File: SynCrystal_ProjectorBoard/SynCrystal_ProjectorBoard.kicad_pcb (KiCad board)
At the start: 2 copper layers, 59.7 x 25.4 mm, 19 parts, among them J1 to Motor Ctrl PCB, J2 to DIN Connector, J3 to Lamp Relay Board, J4 to DIN Socket, J5 Relais Board, J6 uC Cable, U1 AP63205WU, U2 TS5A3160DBVR-TP, U3 TS5A3160DBVR-TP, U4 TS5A3160DBVR-TP

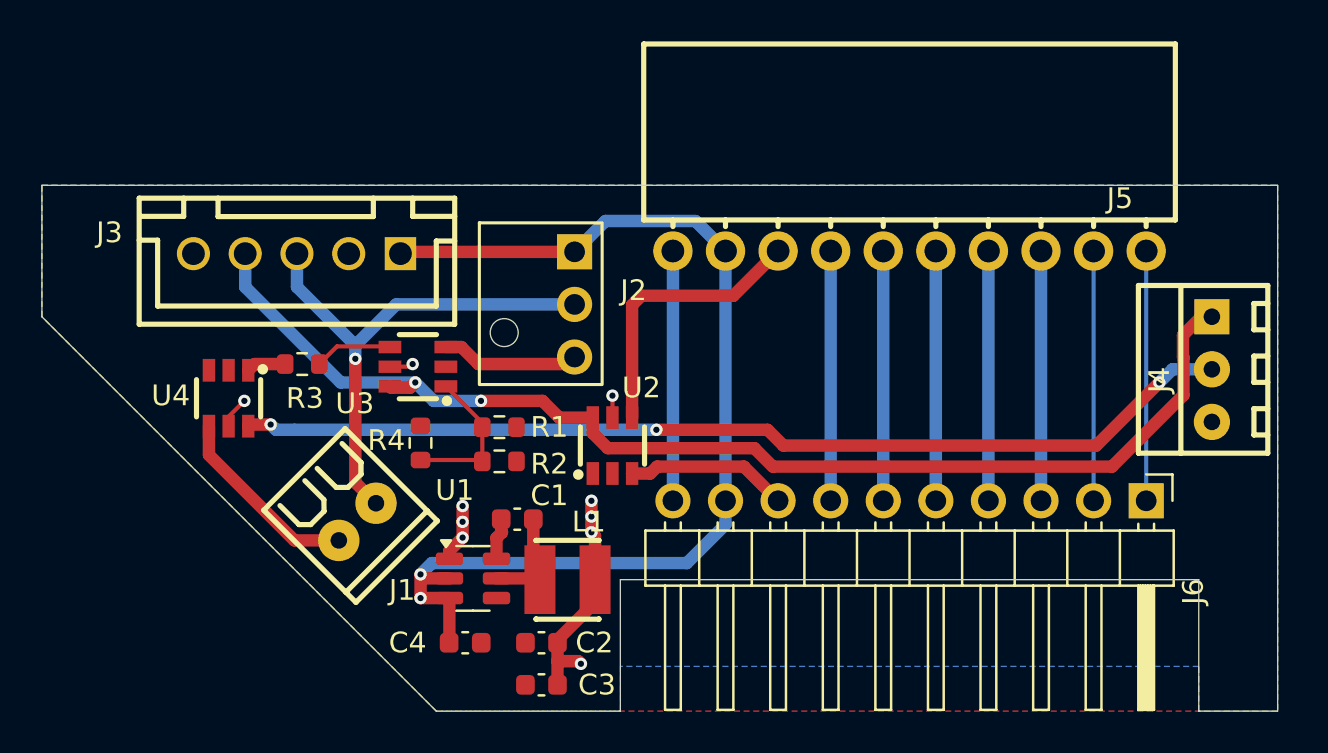
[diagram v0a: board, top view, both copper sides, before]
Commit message: DRC for Projector Board happy
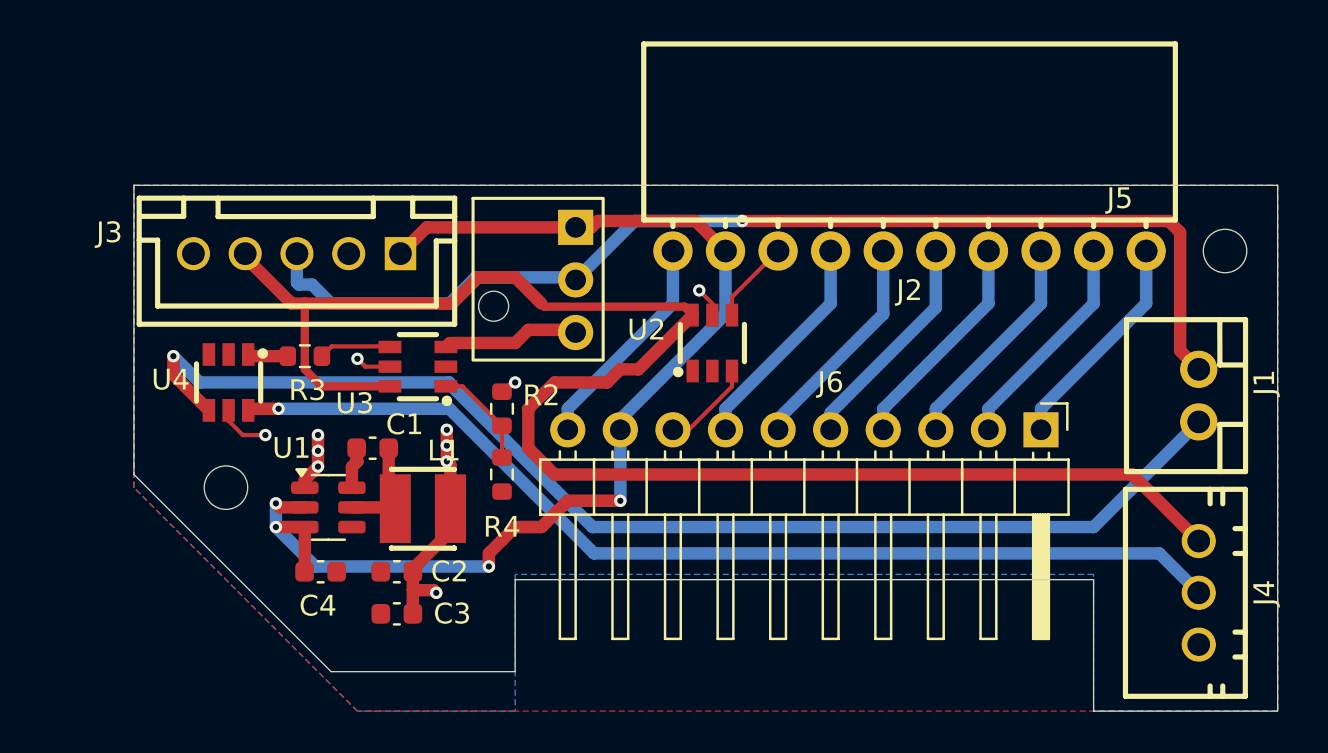
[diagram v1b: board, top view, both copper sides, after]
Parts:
- removed R1: 16k5, Resistor_SMD:R_0603_1608Metric
- added H1: MountingHole, Peacemans Teile:MountingHole_2.1mm_just_hole, F.Cu at (167.6, 90.8)
- added H2: MountingHole, Peacemans Teile:MountingHole_2.1mm_just_hole, F.Cu at (215.9, 79.4)
- J1: footprint easyEDA:CONN-TH_2P-P2.54_MX128-2.54-GN01-02P-CU-Y-A -> easyEDA:CONN-TH_2P-P2.54_ZX-XH2.54-2PZZ-Y
- J4: footprint easyEDA:CONN-TH_3P-P2.54_MX128-2.54-03P-GN01-CU-Y-A -> easyEDA:CONN-TH_ZX-XH2.54-3PZZ-Y
- R2: value 5k1 -> 6k8
- R4: value 1k6 -> 2k7
- moved J1 41.1 mm to (214.6, 86.4), turned to 90 degrees
- moved J4 10.8 mm to (214.6, 95.9)
- moved C4 7.78 mm to (172.2, 94.9)
- moved L1 7.78 mm to (177.2, 91.8)
- moved C1 7.78 mm to (174.7, 88.9)
- moved U1 7.78 mm to (172.6, 91.8)
- moved C2 7.78 mm to (175.9, 94.9)
- moved C3 7.78 mm to (175.9, 96.9)
- moved U2 6.92 mm to (191.1, 83.8)
- moved J6 6.13 mm to (207.0, 88.0)
- moved R4 4.22 mm to (181.0, 90.2), turned to 90 degrees
- moved R2 2.54 mm to (181.0, 87.0), turned to 90 degrees
- moved J2 1.18 mm to (184.5, 78.2)
- moved U4 0.76 mm to (167.8, 85.7)
- moved R3 0.40 mm to (171.4, 84.5)
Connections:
- R2 pad 2: +15V -> +5V
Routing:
- net /Pin_678: track 9.37 -> 58.4 mm, vias 0 -> 1
- net /M-Pin: track 25.0 -> 53.5 mm
- net /Stop_EN: track 58.4 -> 77.6 mm, vias 2 -> 0
- net Net-(J5-Pin_8): track 13.6 -> 4.02 mm
- net +15V: track 52.1 -> 56.4 mm, vias 2 -> 4
- net Net-(J6-Pin_8): track 7.87 -> 4.47 mm
- net +5V: track 17.5 -> 20.3 mm, vias 10 -> 11
- net Net-(R2-Pad1): track 7.36 -> 5.03 mm
- net Net-(J5-Pin_7): track 12.1 -> 10.7 mm
- net Net-(J5-Pin_6): track 12.1 -> 10.7 mm
- net Net-(J5-Pin_3): track 12.1 -> 10.7 mm
- net Net-(J5-Pin_10): track 12.1 -> 10.7 mm
- net Net-(J5-Pin_4): track 12.1 -> 10.7 mm
- net Net-(J5-Pin_2): track 12.1 -> 10.7 mm
- net Net-(J5-Pin_1): track 12.1 -> 10.7 mm
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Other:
- board size 59.7 x 25.4 mm -> 55.2 x 25.4 mm

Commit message: Polishing up for Rev.A
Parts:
- moved U2 2.74 mm to (188.6, 82.8)
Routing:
- net /Stop_EN: track 77.6 -> 73.0 mm
- net Net-(J5-Pin_8): track 4.02 -> 5.63 mm
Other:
- board text added: "Bauer T610 / T525"
- board text added: "JLCJLCJLCJLC"
- board text added: "Red Connector"
- board text added: "Relais-Board"
- board text added: "Rev.A"
- board text added: "SynCrystal Projector Board for Bauer T610 / T525"
- board text added: "by filmkorn.org"
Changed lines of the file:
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@@
 	(footprint "easyEDA:SOT-23-6_L2.9-W1.6-P0.95-LS2.8-BR"
 		(layer "F.Cu")
-		(at 191.135 83.82 -90)
+		(at 188.595 82.804 -90)
 		(property "Reference" "U2"
-			(at -0.635 3.175 360)
+			(at 0 0 360)
 			(layer "F.SilkS")
 			(effects
@@
 		(tags "Through hole pin header THT 1x03 2.54mm single row")
 		(property "Reference" "J2"
-			(at 16.129 3.048 0)
+			(at -2.286 0.508 0)
 			(layer "F.SilkS")
 			(effects
@@
 		(at 167.767 85.725 90)
 		(property "Reference" "U4"
-			(at 0.127 -2.794 180)
+			(at -2.54 -2.667 180)
 			(layer "F.SilkS")
 			(effects
@@
 		(at 171.069 79.502 180)
 		(property "Reference" "J3"
-			(at 9.057 1.016 360)
+			(at 5.969 -4.318 360)
 			(layer "F.SilkS")
 			(effects
@@
 		(at 214.63 86.359999 90)
 		(property "Reference" "J1"
-			(at 0.634999 3.175 90)
+			(at -0.000001 -4.445 90)
 			(layer "F.SilkS")
 			(effects
@@
 		(at 200.66 79.375 180)
 		(property "Reference" "J5"
-			(at -10.16 2.54 360)
+			(at 13.335 0 360)
 			(layer "F.SilkS")
 			(effects
@@
 		(at 214.63 95.885 -90)
 		(property "Reference" "J4"
-			(at 0 -3.175 90)
+			(at -2.54 4.445 90)
 			(layer "F.SilkS")
 			(effects
@@
 		(tags "Through hole angled pin header THT 1x10 2.54mm single row")
 		(property "Reference" "J6"
-			(at -2.286 10.16 180)
+			(at -1.651 21.59 180)
 			(layer "F.SilkS")
 			(effects
@@
 		)
 	)
+	(gr_rect
+		(start 164.465 81.28)
+		(end 179.154876 88.984876)
+		(stroke
+			(width 0.1)
+			(type solid)
+		)
+		(fill solid)
+		(layer "B.SilkS")
+	)
+	(gr_poly
+		(pts
+			(xy 192.532 81.915) (xy 193.802 80.645) (xy 195.072 81.915)
+		)
+		(stroke
+			(width 0.1)
+			(type solid)
+		)
+		(fill solid)
+		(layer "F.SilkS")
+	)
+	(gr_poly
+		(pts
+			(xy 206.502 81.915) (xy 207.772 80.645) (xy 209.042 81.915)
+		)
+		(stroke
+			(width 0.1)
+			(type solid)
+		)
+		(fill solid)
+		(layer "F.SilkS")
+	)
+	(gr_poly
+		(pts
+			(xy 189.23 85.598) (xy 187.96 86.868) (xy 186.69 85.598)
+		)
+		(stroke
+			(width 0.1)
+			(type solid)
+		)
+		(fill solid)
+		(layer "F.SilkS")
+	)
+	(gr_poly
+		(pts
+			(xy 204.47 85.598) (xy 203.2 86.868) (xy 201.93 85.598)
+		)
+		(stroke
+			(width 0.1)
+			(type solid)
+		)
+		(fill solid)
+		(layer "F.SilkS")
+	)
 	(gr_poly
 		(pts
@@
 		(layer "Edge.Cuts")
 	)
+	(gr_text "SynCrystal Projector Board for Bauer T610 / T525"
+		(at 172.085 91.44 0)
+		(layer "B.SilkS")
+		(effects
+			(font
+				(size 1 1)
+				(thickness 0.2)
+				(bold yes)
+			)
+			(justify right bottom mirror)
+		)
+	)
+	(gr_text "by filmkorn.org"
+		(at 172.085 93.98 0)
+		(layer "B.SilkS")
+		(effects
+			(font
+				(size 1 1)
+				(thickness 0.2)
+				(bold yes)
+			)
+			(justify right bottom mirror)
+		)
+	)
+	(gr_text "Rev.A"
+		(at 180.594 98.552 0)
+		(layer "B.SilkS")
+		(effects
+			(font
+				(size 1 1)
+				(thickness 0.1)
+			)
+			(justify left bottom mirror)
+		)
+	)
+	(gr_text "JLCJLCJLCJLC"
+		(at 172.212 77.978 0)
+		(layer "B.SilkS")
+		(effects
+			(font
+				(size 0.8 0.8)
+				(thickness 0.1)
+			)
+			(justify left bottom mirror)
+		)
+	)
+	(gr_text "Relais-Board"
+		(at 195.707 81.915 0)
+		(layer "F.SilkS" knockout)
+		(effects
+			(font
+				(size 1 1)
+				(thickness 0.1)
+			)
+			(justify left bottom)
+		)
+	)
+	(gr_text "Bauer T610 / T525"
+		(at 192.532 84.328 0)
+		(layer "F.SilkS")
+		(effects
+			(font
+				(size 1 1)
+				(thickness 0.1)
+			)
+			(justify left bottom)
+		)
+	)
+	(gr_text "Red Connector"
+		(at 195.58 86.868 0)
+		(layer "F.SilkS" knockout)
+		(effects
+			(font
+				(size 1 1)
+				(thickness 0.1)
+			)
+			(justify bottom)
+		)
+	)
 	(segment
 		(start 173.723 90.81)
@@
 	)
 	(segment
-		(start 191.135 82.47)
-		(end 191.135 81.915)
+		(start 188.595 80.704)
+		(end 188.155 80.264)
+		(width 0.2)
+		(layer "F.Cu")
+		(net 4)
+	)
+	(segment
+		(start 188.155 80.264)
+		(end 187.706 80.264)
 		(width 0.2)
 		(layer "F.Cu")
@@
 	)
 	(segment
-		(start 191.135 81.915)
-		(end 190.5 81.28)
+		(start 188.595 81.454)
+		(end 188.595 80.704)
 		(width 0.2)
 		(layer "F.Cu")
@@
 	)
 	(via
-		(at 172.085 88.265)
+		(at 187.706 80.264)
 		(size 0.6)
 		(drill 0.3)
@@
 	)
 	(via
-		(at 181.61 85.725)
+		(at 172.085 88.265)
 		(size 0.6)
 		(drill 0.3)
@@
 	)
 	(via
-		(at 169.545 88.265)
+		(at 181.61 85.725)
 		(size 0.6)
 		(drill 0.3)
@@
 	)
 	(via
-		(at 178.308 89.535)
+		(at 169.545 88.265)
 		(size 0.6)
 		(drill 0.3)
@@
 	)
 	(via
-		(at 178.308 88.011)
+		(at 178.308 89.535)
 		(size 0.6)
 		(drill 0.3)
@@
 	)
 	(via
-		(at 172.085 89.027)
+		(at 178.308 88.011)
 		(size 0.6)
 		(drill 0.3)
@@
 	)
 	(via
-		(at 190.5 81.28)
+		(at 172.085 89.027)
 		(size 0.6)
 		(drill 0.3)
@@
 	)
 	(segment
-		(start 183.515 90.17)
-		(end 211.415 90.17)
+		(start 211.415 90.17)
+		(end 214.63 93.385)
 		(width 0.6)
 		(layer "F.Cu")
@@
 	)
 	(segment
-		(start 189.777 82.062)
-		(end 183.027 82.062)
-		(width 0.4)
-		(layer "F.Cu")
-		(net 9)
-	)
-	(segment
 		(start 178.557 81.915)
 		(end 179.827 80.645)
@@
 	)
 	(segment
-		(start 182.245 88.9)
-		(end 183.515 90.17)
+		(start 184.15 85.09)
+		(end 182.245 86.995)
 		(width 0.6)
 		(layer "F.Cu")
@@
 	)
 	(segment
-		(start 183.027 82.062)
-		(end 182.88 81.915)
-		(width 0.4)
-		(layer "F.Cu")
-		(net 9)
-	)
-	(segment
 		(start 177.165 81.915)
 		(end 178.557 81.915)
@@
 	)
 	(segment
-		(start 186.69 85.09)
-		(end 186.055 85.725)
-		(width 0.6)
-		(layer "F.Cu")
-		(net 9)
-	)
-	(segment
-		(start 182.245 86.995)
-		(end 182.245 88.9)
-		(width 0.6)
-		(layer "F.Cu")
-		(net 9)
-	)
-	(segment
 		(start 181.61 80.645)
 		(end 182.88 81.915)
@@
 	)
 	(segment
+		(start 187.325 82.062)
+		(end 183.027 82.062)
+		(width 0.4)
+		(layer "F.Cu")
+		(net 9)
+	)
+	(segment
 		(start 171.45 81.915)
 		(end 177.165 81.915)
@@
 	)
 	(segment
+		(start 183.027 82.062)
+		(end 182.88 81.915)
+		(width 0.4)
+		(layer "F.Cu")
+		(net 9)
+	)
+	(segment
+		(start 187.645 82.47)
+		(end 185.025 85.09)
+		(width 0.6)
+		(layer "F.Cu")
+		(net 9)
+	)
+	(segment
 		(start 170.815 81.915)
 		(end 171.45 81.915)
@@
 	)
 	(segment
-		(start 186.055 85.725)
-		(end 183.515 85.725)
+		(start 185.025 85.09)
+		(end 184.15 85.09)
 		(width 0.6)
 		(layer "F.Cu")
@@
 	)
 	(segment
-		(start 187.565 85.09)
-		(end 186.69 85.09)
+		(start 183.515 90.17)
+		(end 211.415 90.17)
 		(width 0.6)
 		(layer "F.Cu")
@@
 	)
 	(segment
-		(start 183.515 85.725)
-		(end 182.245 86.995)
+		(start 187.645 81.454)
+		(end 187.645 82.47)
 		(width 0.6)
 		(layer "F.Cu")
@@
 	)
 	(segment
-		(start 190.185 82.47)
-		(end 189.777 82.062)
-		(width 0.4)
-		(layer "F.Cu")
-		(net 9)
-	)
-	(segment
-		(start 211.415 90.17)
-		(end 214.63 93.385)
+		(start 182.245 88.9)
+		(end 183.515 90.17)
 		(width 0.6)
 		(layer "F.Cu")
@@
 	)
 	(segment
-		(start 190.185 82.47)
-		(end 187.565 85.09)
+		(start 179.827 80.645)
+		(end 181.61 80.645)
 		(width 0.6)
 		(layer "F.Cu")
@@
 	)
 	(segment
-		(start 179.827 80.645)
-		(end 181.61 80.645)
+		(start 182.245 86.995)
+		(end 182.245 88.9)
 		(width 0.6)
 		(layer "F.Cu")
@@
 	)
 	(segment
-		(start 192.085 81.6)
+		(start 192.231 81.454)
 		(end 194.31 79.375)
-		(width 0.2)
+		(width 0.6)
 		(layer "F.Cu")
 		(net 13)
 	)
 	(segment
-		(start 192.085 82.47)
-		(end 192.085 81.6)
-		(width 0.2)
+		(start 189.545 81.454)
+		(end 192.231 81.454)
+		(width 0.6)
 		(layer "F.Cu")
 		(net 13)
@@
 	)
 	(segment
-		(start 189.994 88.011)
+		(start 189.545 87.696)
 		(end 189.23 88.011)
-		(width 0.2)
-		(layer "F.Cu")
-		(net 23)
-	)
-	(segment
-		(start 192.085 85.92)
-		(end 189.994 88.011)
-		(width 0.2)
+		(width 0.6)
 		(layer "F.Cu")
 		(net 23)
 	)
 	(segment
-		(start 192.085 85.17)
-		(end 192.085 85.92)
-		(width 0.2)
+		(start 189.545 84.154)
+		(end 189.545 87.696)
+		(width 0.6)
 		(layer "F.Cu")
 		(net 23)

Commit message: More changes
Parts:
- removed H1, H2: MountingHole, Peacemans Teile:MountingHole_2.1mm_just_hole
- removed U2: TS5A3160DBVR-TP, easyEDA:SOT-23-6_L2.9-W1.6-P0.95-LS2.8-BR
- added Q1: AO3400A, Package_TO_SOT_SMD:SOT-23, F.Cu at (190.4, 82.5)
- added R1: 220, Resistor_SMD:R_0603_1608Metric, F.Cu at (190.1, 85.2)
- added R5: 10k, Resistor_SMD:R_0603_1608Metric, F.Cu at (187.5, 82.3)
- added R6: 10k, Resistor_SMD:R_0603_1608Metric, F.Cu at (193.9, 82.3)
- J1: value to Motor Ctrl PCB -> to TCA955 PCB
- J2: value to DIN Connector -> to DIN connecting 3+1 Socket plug
- J4: value to DIN Socket -> to DIN Socket traces
- moved J4 1.65 mm to (214.6, 94.2)
- moved J1 1.52 mm to (214.6, 84.8)
- moved R3 1.40 mm to (171.4, 85.9)
- moved U3 1.40 mm to (176.9, 86.4)
- moved U4 1.40 mm to (167.8, 87.1)
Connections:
- J4 pad 3: unconnected-(J4-Pin_3-Pad3) -> GND
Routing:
- net Net-(Q1-G): track 0.00 -> 6.28 mm
- net Net-(J6-Pin_8): track 3.99 -> 7.65 mm
- net /Pin_678: track 58.4 -> 55.9 mm
- net /Stop_EN: track 73.0 -> 74.9 mm
- net /M-Pin: track 53.5 -> 51.9 mm
- net +5V: track 20.6 -> 22.2 mm, vias 11 -> 9
- net /DAC_EN: track 49.6 -> 48.6 mm
- net Net-(R2-Pad1): track 5.03 -> 4.45 mm
- net /Ctrl_V_in: track 6.67 -> 7.24 mm
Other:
- board size 55.2 x 25.4 mm -> 54.4 x 23.5 mm
- board text added: "Bauer T610/T525"
- board text added: "DIN Traces"
- board text added: "Lamp Relais"
- board text added: "M"
- board text added: "TCA955"
- board text removed: "Bauer T610 / T525"
- board text removed: "Red Connector"
- board text removed: "Relais-Board"

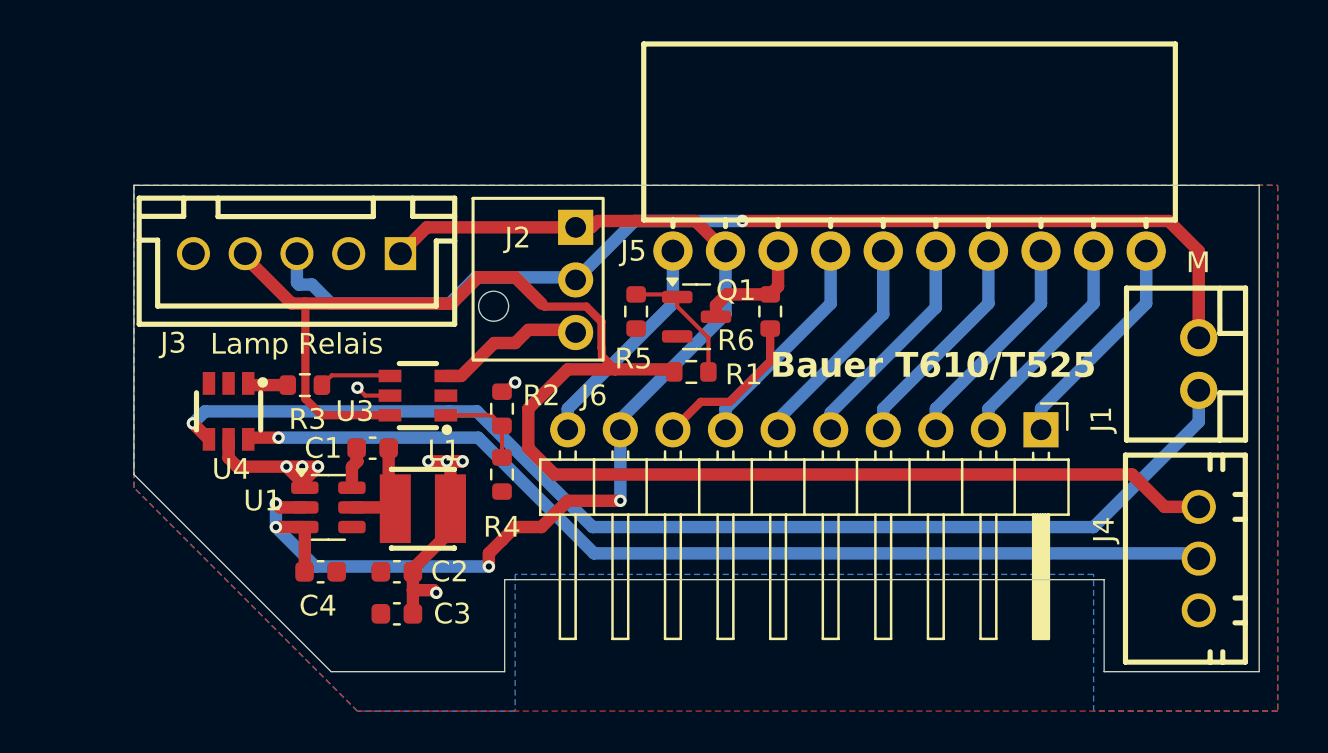
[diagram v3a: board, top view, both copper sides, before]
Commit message: Moved the OpAmp to the Projector Board. This Layout is DRC 0, but not optimal
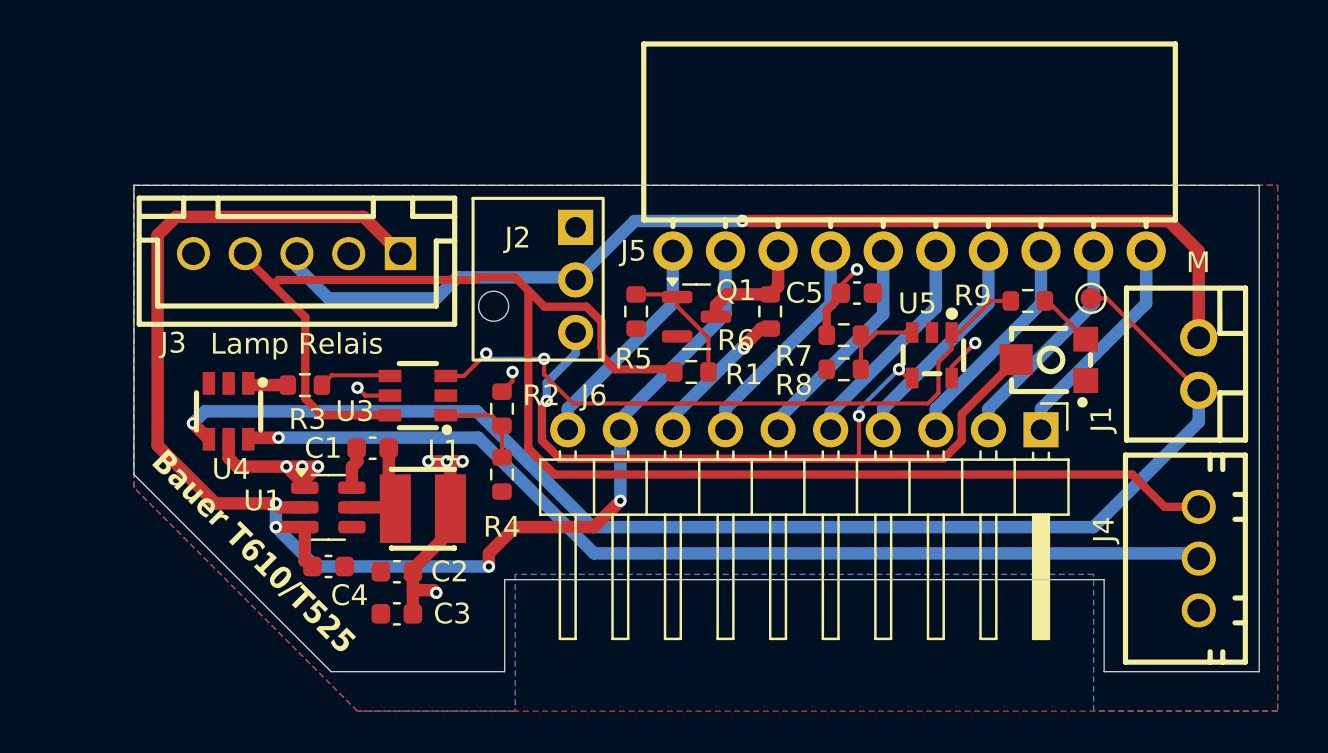
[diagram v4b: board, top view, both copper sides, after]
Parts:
- added C5: 100n, Capacitor_SMD:C_0603_1608Metric, F.Cu at (198.1, 81.4)
- added R7: 10k, Resistor_SMD:R_0603_1608Metric, F.Cu at (197.5, 83.4)
- added R8: 4k7, Resistor_SMD:R_0603_1608Metric, F.Cu at (197.5, 85.1)
- added R9: 2k7, Resistor_SMD:R_0603_1608Metric, F.Cu at (206.4, 81.8)
- added RV1: 300, easyEDA:RES-ADJ-SMD_3P-L3.8-W3.7_VGF39NCHXT, F.Cu at (207.5, 84.6)
- added TP1: 678, TestPoint:TestPoint_Pad_D1.0mm, F.Cu at (209.4, 81.7)
- added U5: TSV911ILT, easyEDA:SOT-23-5_L2.9-W1.6-P0.95-LS2.8-BR, F.Cu at (201.7, 84.4)
- J2: value to DIN connecting 3+1 Socket plug -> to DIN connecting 3+1 Socket cable
- moved C4 0.46 mm to (172.6, 94.6)
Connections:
- J2 pad 1: +15V -> +5V
- U3 pad 3: /Ctrl_V_in -> Net-(R9-Pad1)
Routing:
- net Net-(R9-Pad1): track 0.00 -> 32.6 mm, vias 0 -> 2
- net /Ctrl_V_in: track 7.24 -> 37.9 mm, vias 0 -> 3
- net +15V: track 56.4 -> 68.8 mm
- net /Pin_678: track 55.9 -> 62.9 mm
- net +5V: track 22.2 -> 28.4 mm, vias 9 -> 11
- net Net-(U5-+): track 0.00 -> 3.81 mm
- net Net-(R9-Pad2): track 0.00 -> 2.74 mm
- net /Stop_EN: track 74.9 -> 76.4 mm
- net /M-Pin: track 51.9 -> 51.3 mm
- net Net-(J6-Pin_8): track 7.65 -> 7.17 mm, vias 0 -> 1

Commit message: Much better layout, DRC = 0
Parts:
- moved U4 39.7 mm to (207.3, 82.8), turned to 180 degrees
- moved R3 31.2 mm to (202.4, 82.0), turned to 0 degrees
- moved R8 30.7 mm to (166.8, 85.0), turned to 90 degrees
- moved U5 29.5 mm to (172.2, 85.1)
- moved R9 29.3 mm to (177.2, 83.9)
- moved RV1 28.9 mm to (178.7, 86.6)
- moved R7 28.5 mm to (169.0, 85.0), turned to -90 degrees
- moved C5 27.4 mm to (171.6, 88.0), turned to 180 degrees
- moved R4 20.2 mm to (199.6, 82.5), turned to -90 degrees
- moved U3 19.9 mm to (196.6, 83.3), turned to 90 degrees
- moved R2 19.5 mm to (200.4, 85.2), turned to 0 degrees
- moved TP1 3.95 mm to (209.7, 85.6)
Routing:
- net /Pin_678: track 62.9 -> 9.27 mm, vias 1 -> 0
- net /DAC_EN: track 48.6 -> 16.4 mm
- net /Ctrl_V_in: track 37.9 -> 17.2 mm, vias 3 -> 2
- net GND: track 10.7 -> 0.00 mm
- net Net-(R3-Pad1): track 3.49 -> 11.1 mm
- net /M-Pin: track 51.3 -> 54.1 mm
- net +5V: track 28.4 -> 30.3 mm, vias 11 -> 10
- net Net-(R9-Pad1): track 32.6 -> 31.3 mm
- net Net-(R3-Pad2): track 1.94 -> 2.73 mm
- net Net-(U5-+): track 3.81 -> 4.57 mm
- net +15V: track 68.8 -> 68.1 mm
